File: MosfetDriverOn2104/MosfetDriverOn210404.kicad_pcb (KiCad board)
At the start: 2 copper layers, 22 parts, among them J1 Screw_Terminal_01x02, J10 CROSS CONN, J11 Screw_Terminal_01x03, J2 AVR-ISP-6, J3 I2C HDR, J4 I2C HDR, J5 UART HDR, J6 I2C HDR, J7 5V HDR, J8 ENCODER HDR, J9 GND HDR, SW1 SW_Push_Dual, SW2 SW1, SW3 SW2

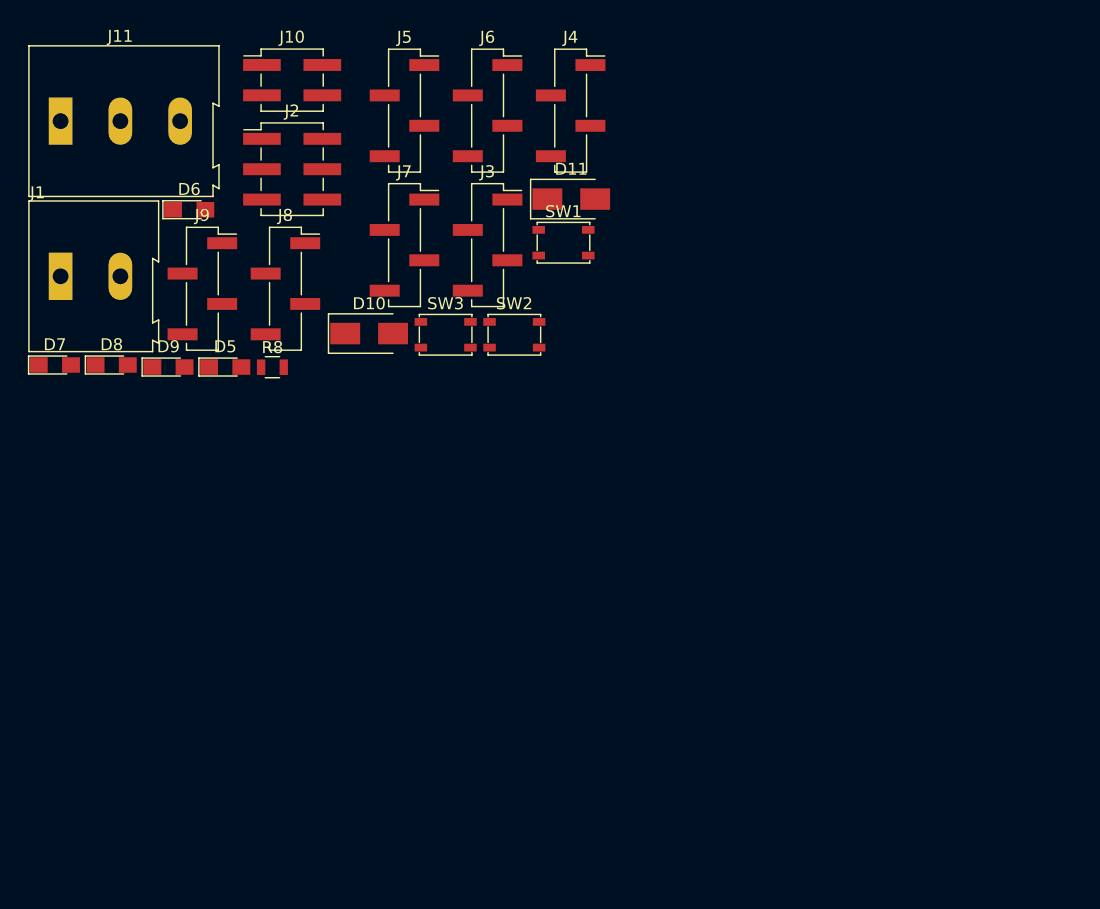
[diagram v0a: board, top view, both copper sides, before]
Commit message: #4 ,switches footprints also changed to THT
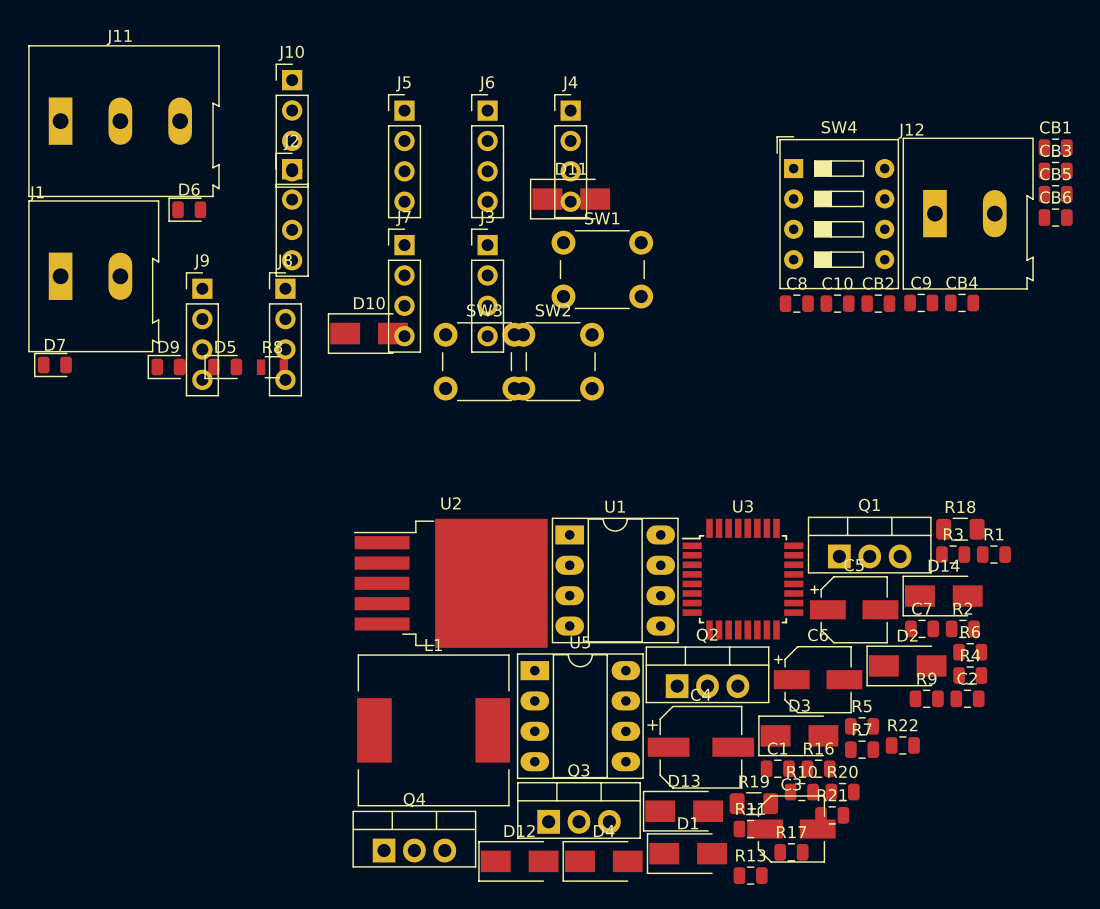
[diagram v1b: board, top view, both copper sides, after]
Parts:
- removed D8: LED, LEDs:LED_0805_HandSoldering
- added C1: C_Small, Capacitor_SMD:C_0805_2012Metric, F.Cu at (161.4, 92.3)
- added C10: 22u, Capacitor_SMD:C_0805_2012Metric, F.Cu at (166.4, 53.4)
- added C2: C_Small, Capacitor_SMD:C_0805_2012Metric, F.Cu at (177.3, 86.5)
- added C3: CP_Small, Capacitor_SMD:CP_Elec_5x4.4, F.Cu at (162.5, 97.3)
- added C4: CP, Capacitor_SMD:CP_Elec_6.3x5.7, F.Cu at (155.0, 90.5)
- added C5: CP, Capacitor_SMD:CP_Elec_5x5.4, F.Cu at (167.8, 79.0)
- added C6: CP, Capacitor_SMD:CP_Elec_5x5.4, F.Cu at (164.8, 84.9)
- added C7: C, Capacitor_SMD:C_0805_2012Metric, F.Cu at (173.5, 80.6)
- added C8: C_Small, Capacitor_SMD:C_0805_2012Metric, F.Cu at (163.0, 53.4)
- added C9: 22u, Capacitor_SMD:C_0805_2012Metric, F.Cu at (173.4, 53.3)
- added CB1: .1, Capacitor_SMD:C_0805_2012Metric, F.Cu at (184.6, 40.3)
- added CB2: .1u, Capacitor_SMD:C_0805_2012Metric, F.Cu at (169.8, 53.4)
- added CB3: 1uF, Capacitor_SMD:C_0805_2012Metric, F.Cu at (184.6, 42.3)
- added CB4: .1uF, Capacitor_SMD:C_0805_2012Metric, F.Cu at (176.8, 53.3)
- added CB5: 1uF, Capacitor_SMD:C_0805_2012Metric, F.Cu at (184.6, 44.2)
- added CB6: .1uF, Capacitor_SMD:C_0805_2012Metric, F.Cu at (184.6, 46.2)
- added D1: D, Diode_SMD:D_SMA, F.Cu at (153.9, 99.4)
- added D12: D, Diode_SMD:D_SMA, F.Cu at (139.8, 100.1)
- added D13: D, Diode_SMD:D_SMA, F.Cu at (153.6, 95.9)
- added D14: D, Diode_SMD:D_SMA, F.Cu at (175.3, 77.9)
- added D2: D, Diode_SMD:D_SMA, F.Cu at (172.3, 83.7)
- added D3: D, Diode_SMD:D_SMA, F.Cu at (163.2, 89.6)
- added D4: SS24, Diode_SMD:D_SMA, F.Cu at (146.9, 100.1)
- added J12: motor, TerminalBlock:TerminalBlock_Altech_AK300-2_P5.00mm, F.Cu at (174.6, 45.9)
- added L1: 220uH, Inductor_SMD:L_12x12mm_H6mm, F.Cu at (132.6, 89.1)
- added Q1: IRF540N, Package_TO_SOT_THT:TO-220-3_Vertical, F.Cu at (166.6, 74.5)
- added Q2: IRF540N, Package_TO_SOT_THT:TO-220-3_Vertical, F.Cu at (153.0, 85.4)
- added Q3: IRF540N, Package_TO_SOT_THT:TO-220-3_Vertical, F.Cu at (142.2, 96.7)
- added Q4: IRF540N, Package_TO_SOT_THT:TO-220-3_Vertical, F.Cu at (128.5, 99.1)
- added R1: R, Resistor_SMD:R_0805_2012Metric, F.Cu at (179.5, 74.4)
- added R10: 540, Resistor_SMD:R_0805_2012Metric, F.Cu at (163.4, 94.3)
- added R11: 540, Resistor_SMD:R_0805_2012Metric, F.Cu at (159.1, 97.3)
- added R13: 1K, Resistor_SMD:R_0805_2012Metric, F.Cu at (159.1, 101.2)
- added R16: 10K, Resistor_SMD:R_0805_2012Metric, F.Cu at (164.8, 92.3)
- added R17: R, Resistor_SMD:R_0805_2012Metric, F.Cu at (162.5, 99.3)
- added R18: R, Resistor_SMD:R_1206_3216Metric, F.Cu at (176.7, 72.3)
- added R19: R, Resistor_SMD:R_1206_3216Metric, F.Cu at (159.4, 95.2)
- added R2: R, Resistor_SMD:R_0805_2012Metric, F.Cu at (176.9, 80.6)
- added R20: R, Resistor_SMD:R_0805_2012Metric, F.Cu at (166.8, 94.3)
- added R21: R, Resistor_SMD:R_0805_2012Metric, F.Cu at (166.0, 96.2)
- added R22: R, Resistor_SMD:R_0805_2012Metric, F.Cu at (171.9, 90.4)
- added R3: 240, Resistor_SMD:R_0805_2012Metric, F.Cu at (176.1, 74.4)
- added R4: 2k7, Resistor_SMD:R_0805_2012Metric, F.Cu at (177.5, 84.5)
- added R5: 10K, Resistor_SMD:R_0805_2012Metric, F.Cu at (168.5, 88.8)
- added R6: 1K, Resistor_SMD:R_0805_2012Metric, F.Cu at (177.5, 82.6)
- added R7: 4K7, Resistor_SMD:R_0805_2012Metric, F.Cu at (168.5, 90.7)
- added R9: 540, Resistor_SMD:R_0805_2012Metric, F.Cu at (173.9, 86.5)
- added SW4: SW_DIP_x04, Button_Switch_THT:SW_DIP_SPSTx04_Slide_9.78x12.34mm_W7.62mm_P2.54mm, F.Cu at (162.7, 42.1)
- added U1: IR2104, Package_DIP:DIP-8_W7.62mm_Socket_LongPads, F.Cu at (144.0, 72.7)
- added U2: LM2576HVS-ADJ, Package_TO_SOT_SMD:TO-263-5_TabPin3, F.Cu at (134.1, 76.8)
- added U3: ATmega328P-AU-MCU_Microchip_ATmega, Package_QFP:TQFP-32_7x7mm_P0.8mm, F.Cu at (158.5, 76.4)
- added U5: IR2104, Package_DIP:DIP-8_W7.62mm_Socket_LongPads, F.Cu at (141.1, 84.1)
- D5, D6, D9: footprint LEDs:LED_0805_HandSoldering -> LED_SMD:LED_0805_2012Metric
- D7: value LED -> 5.1V; footprint LEDs:LED_0805_HandSoldering -> LED_SMD:LED_0805_2012Metric
- J10: footprint Pin_Headers:Pin_Header_Straight_2x02_Pitch2.54mm_SMD -> Connector_PinHeader_2.54mm:PinHeader_1x04_P2.54mm_Vertical
- J11: value Screw_Terminal_01x03 -> servo hdr
- J2: footprint Pin_Headers:Pin_Header_Straight_2x03_Pitch2.54mm_SMD -> Connector_PinHeader_2.54mm:PinHeader_1x04_P2.54mm_Vertical
- J3, J4, J5, J6, J7, J8, J9: footprint Pin_Headers:Pin_Header_Straight_1x04_Pitch2.54mm_SMD_Pin1Right -> Connector_PinHeader_2.54mm:PinHeader_1x04_P2.54mm_Vertical
- SW1, SW2, SW3: footprint Buttons_Switches_SMD:SW_SPST_PTS810 -> Button_Switch_THT:SW_PUSH_6mm
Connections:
- D5 pad 1: (no net) -> Net-(D5-Pad1)
- D5 pad 2: (no net) -> Net-(D5-Pad2)
- D6 pad 1: (no net) -> Net-(D6-Pad1)
- D6 pad 2: (no net) -> Net-(D6-Pad2)
- D7 pad 1: (no net) -> /~SD
- D7 pad 2: /MISO -> GND
- D9 pad 1: (no net) -> Net-(D9-Pad1)
- J1 pad 2: (no net) -> VCC
- J10 pad 2: (no net) -> /IN1
- J10 pad 3: (no net) -> /IN2
- J11 pad 1: (no net) -> GND
- J11 pad 2: GND -> /svo
- J11 pad 3: (no net) -> +5V
- J2 pad 4: (no net) -> /MOSI
- J5 pad 2: (no net) -> /TX
- J5 pad 3: (no net) -> /RX
- J8 pad 2: (no net) -> /B
- J8 pad 3: (no net) -> /A
- SW2 pad 1: Net-(R10-Pad1) -> +5V

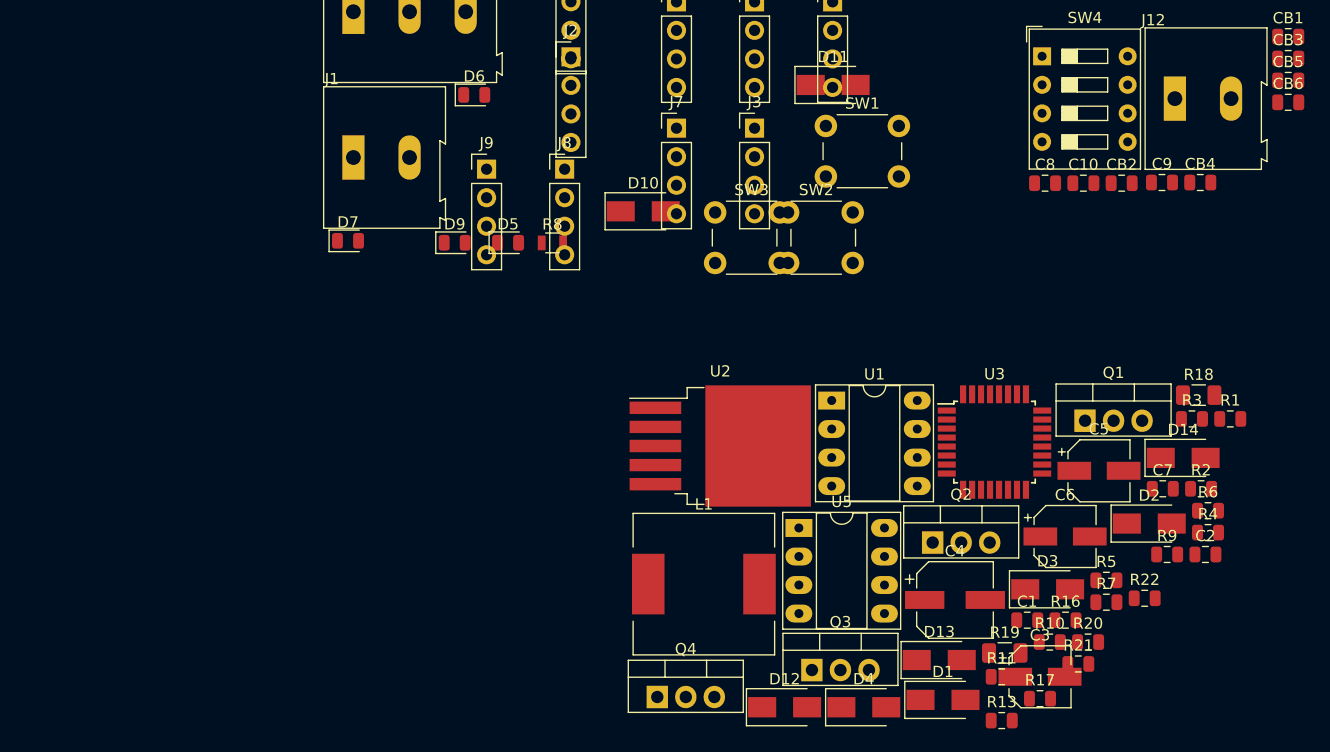
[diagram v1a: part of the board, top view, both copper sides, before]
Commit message: Schematcs updated with mosfet footprints
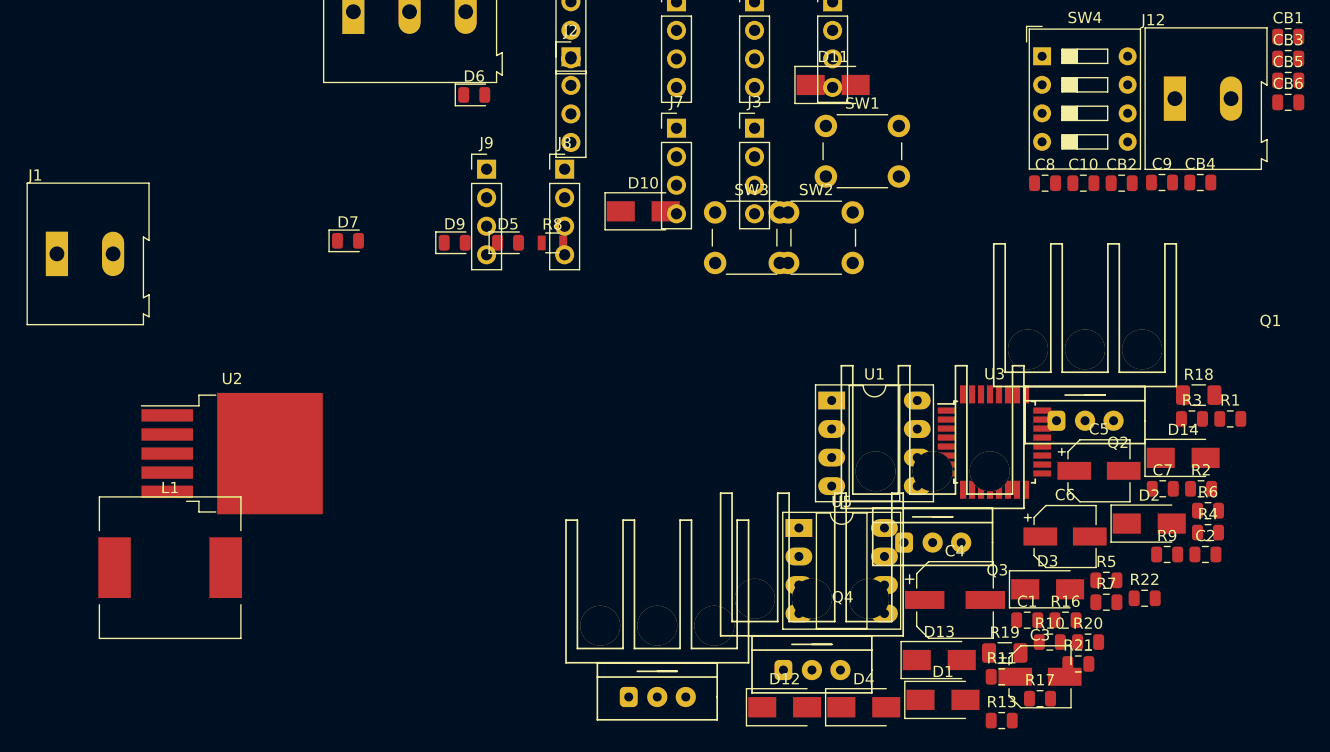
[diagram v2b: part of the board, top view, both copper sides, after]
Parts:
- Q1, Q2, Q3, Q4: footprint Package_TO_SOT_THT:TO-220-3_Vertical -> Footprints:TO220_HS_SCREW
- moved L1 47.5 mm to (85.1, 87.6)
- moved U2 43.5 mm to (90.6, 77.5)
- moved J1 27.8 mm to (75.0, 59.7)

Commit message: starting with pcb, yet to place cpmparator
i am not sure about the D2pack of 7805ic
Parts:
- removed R16: 10K, Resistor_SMD:R_0805_2012Metric
- added C11: 220uF, Capacitor_SMD:CP_Elec_5x4.4, F.Cu at (70.2, 41.9)
- added C12: 440uF, Capacitor_SMD:CP_Elec_5x4.4, F.Cu at (76.5, 48.3)
- added U4: L7805, Package_TO_SOT_SMD:TO-263-3_TabPin2, F.Cu at (230.3, 36.8)
- C8: value C_Small -> .1uF
- D7: footprint LED_SMD:LED_0805_2012Metric -> Diode_SMD:D_SMA
- J2: footprint Connector_PinHeader_2.54mm:PinHeader_1x04_P2.54mm_Vertical -> Connector_PinHeader_2.54mm:PinHeader_2x03_P2.54mm_Vertical
- SW1, SW2, SW3: footprint Button_Switch_THT:SW_PUSH_6mm -> Button_Switch_THT:SW_TH_Tactile_Omron_B3F-10xx
- moved R4 141.0 mm to (38.4, 108.0)
- moved R3 135.0 mm to (44.1, 102.9)
- moved D9 133.8 mm to (239.7, 24.1)
- moved Q3 127.7 mm to (130.8, -30.5)
- moved CB1 125.1 mm to (171.9, -84.1)
- moved CB5 125.1 mm to (171.9, -80.2)
- moved CB6 125.1 mm to (171.9, -78.3)
- moved D11 125.1 mm to (131.4, -79.8)
- moved D14 125.1 mm to (162.6, -46.6)
- moved J12 125.1 mm to (161.9, -78.6)
- moved Q1 125.1 mm to (153.9, -49.9)
- moved R1 125.1 mm to (166.8, -50.1)
- moved R17 125.1 mm to (149.8, -25.2)
- moved R18 125.1 mm to (164.0, -52.2)
- moved R22 125.1 mm to (159.2, -34.1)
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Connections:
- SW3 pad 1: Net-(R16-Pad1) -> +5V
- SW4 pad 5: +5V -> GND
- SW4 pad 6: +5V -> GND
- SW4 pad 7: +5V -> GND
- SW4 pad 8: +5V -> GND
- U3 pad 9: Net-(R16-Pad1) -> +5V
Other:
- board outline added: 99.8 x 100.6 mm

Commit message: fixes #4 , #3 ,
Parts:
- moved Q1 80.8 mm to (81.5, -14.0), turned to 180 degrees
- moved U1 61.0 mm to (70.4, -55.4)
- moved Q3 49.0 mm to (82.0, -25.9)
- moved Q2 48.7 mm to (98.6, -14.0), turned to 180 degrees
- moved D7 28.8 mm to (65.5, -48.3), turned to 270 degrees
- moved Q4 15.9 mm to (99.8, -25.4)
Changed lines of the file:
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@@
   )
   (module Package_DIP:DIP-8_W7.62mm_Socket_LongPads (layer F.Cu)
-    (at 131.295001 -51.714999)
+    (at 70.358 -55.372)
     (descr "8-lead though-hole mounted DIP package, row spacing 7.62 mm (300 mils), Socket, LongPads")
     (tags "THT DIP DIL PDIP 2.54mm 7.62mm 300mil Socket LongPads")
@@
   )
   (module Footprints:TO220_HS_SCREW (layer F.Cu)
-    (at 153.855001 -49.914999)
-    (fp_text reference Q1 (at 16.51 -8.89) (layer F.SilkS)
-      (effects (font (size 1 1) (thickness 0.15)))
-    )
-    (fp_text value IRF540N (at 2.54 -7.62) (layer F.Fab)
+    (at 81.534 -13.97 180)
+    (fp_text reference Q1 (at 16.51 -8.89 180) (layer F.SilkS)
+      (effects (font (size 1 1) (thickness 0.15)))
+    )
+    (fp_text value IRF540N (at 2.54 -7.62 180) (layer F.Fab)
       (effects (font (size 1 1) (thickness 0.15)))
     )
@@
     (fp_line (start 5.334 -3.048) (end -5.334 -3.048) (layer F.SilkS) (width 0.15))
     (fp_line (start 5.334 0) (end 5.334 -3.048) (layer F.SilkS) (width 0.15))
-    (pad 2 thru_hole circle (at 0 -6.35) (size 3.556 3.556) (drill 3.556) (layers *.Cu *.Mask)
+    (pad 2 thru_hole circle (at 0 -6.35 180) (size 3.556 3.556) (drill 3.556) (layers *.Cu *.Mask)
       (net 25 VCC))
-    (pad 2 thru_hole circle (at -5.08 -6.35) (size 3.556 3.556) (drill 3.556) (layers *.Cu *.Mask)
+    (pad 2 thru_hole circle (at -5.08 -6.35 180) (size 3.556 3.556) (drill 3.556) (layers *.Cu *.Mask)
       (net 25 VCC))
-    (pad 2 thru_hole circle (at 5.08 -6.35) (size 3.556 3.556) (drill 3.556) (layers *.Cu *.Mask)
+    (pad 2 thru_hole circle (at 5.08 -6.35 180) (size 3.556 3.556) (drill 3.556) (layers *.Cu *.Mask)
       (net 25 VCC))
-    (pad 3 thru_hole circle (at 2.54 0) (size 1.8 1.8) (drill 0.8) (layers *.Cu *.Mask)
+    (pad 3 thru_hole circle (at 2.54 0 180) (size 1.8 1.8) (drill 0.8) (layers *.Cu *.Mask)
       (net 34 /M1))
-    (pad 2 thru_hole circle (at 0 0) (size 1.8 1.8) (drill 0.8) (layers *.Cu *.Mask)
+    (pad 2 thru_hole circle (at 0 0 180) (size 1.8 1.8) (drill 0.8) (layers *.Cu *.Mask)
       (net 25 VCC))
-    (pad 1 thru_hole roundrect (at -2.54 0) (size 1.6 1.8) (drill 0.8) (layers *.Cu *.Mask) (roundrect_rratio 0.25)
+    (pad 1 thru_hole roundrect (at -2.54 0 180) (size 1.6 1.8) (drill 0.8) (layers *.Cu *.Mask) (roundrect_rratio 0.25)
       (net 11 "Net-(D2-Pad2)"))
   )
   (module Footprints:TO220_HS_SCREW (layer F.Cu)
-    (at 140.285001 -39.064999)
-    (fp_text reference Q2 (at 16.51 -8.89) (layer F.SilkS)
-      (effects (font (size 1 1) (thickness 0.15)))
-    )
-    (fp_text value IRF540N (at 2.54 -7.62) (layer F.Fab)
+    (at 98.552 -13.97 180)
+    (fp_text reference Q2 (at 16.51 -8.89 180) (layer F.SilkS)
+      (effects (font (size 1 1) (thickness 0.15)))
+    )
+    (fp_text value IRF540N (at 2.54 -7.62 180) (layer F.Fab)
       (effects (font (size 1 1) (thickness 0.15)))
     )
@@
     (fp_line (start -2.032 -4.318) (end 2.032 -4.318) (layer F.SilkS) (width 0.15))
     (fp_line (start 3.048 -4.318) (end 7.112 -4.318) (layer F.SilkS) (width 0.15))
-    (pad 1 thru_hole roundrect (at -2.54 0) (size 1.6 1.8) (drill 0.8) (layers *.Cu *.Mask) (roundrect_rratio 0.25)
+    (pad 1 thru_hole roundrect (at -2.54 0 180) (size 1.6 1.8) (drill 0.8) (layers *.Cu *.Mask) (roundrect_rratio 0.25)
       (net 14 "Net-(D3-Pad2)"))
-    (pad 2 thru_hole circle (at 0 0) (size 1.8 1.8) (drill 0.8) (layers *.Cu *.Mask)
+    (pad 2 thru_hole circle (at 0 0 180) (size 1.8 1.8) (drill 0.8) (layers *.Cu *.Mask)
       (net 34 /M1))
-    (pad 3 thru_hole circle (at 2.54 0) (size 1.8 1.8) (drill 0.8) (layers *.Cu *.Mask)
+    (pad 3 thru_hole circle (at 2.54 0 180) (size 1.8 1.8) (drill 0.8) (layers *.Cu *.Mask)
       (net 35 /IS+))
-    (pad 2 thru_hole circle (at 5.08 -6.35) (size 3.556 3.556) (drill 3.556) (layers *.Cu *.Mask)
+    (pad 2 thru_hole circle (at 5.08 -6.35 180) (size 3.556 3.556) (drill 3.556) (layers *.Cu *.Mask)
       (net 34 /M1))
-    (pad 2 thru_hole circle (at -5.08 -6.35) (size 3.556 3.556) (drill 3.556) (layers *.Cu *.Mask)
+    (pad 2 thru_hole circle (at -5.08 -6.35 180) (size 3.556 3.556) (drill 3.556) (layers *.Cu *.Mask)
       (net 34 /M1))
-    (pad 2 thru_hole circle (at 0 -6.35) (size 3.556 3.556) (drill 3.556) (layers *.Cu *.Mask)
+    (pad 2 thru_hole circle (at 0 -6.35 180) (size 3.556 3.556) (drill 3.556) (layers *.Cu *.Mask)
       (net 34 /M1))
   )
   (module Footprints:TO220_HS_SCREW (layer F.Cu)
-    (at 130.81 -30.48)
+    (at 82.042 -25.908)
     (fp_text reference Q3 (at 16.51 -8.89) (layer F.SilkS)
       (effects (font (size 1 1) (thickness 0.15)))
@@
   )
   (module Footprints:TO220_HS_SCREW (layer F.Cu)
-    (at 115.765001 -25.314999)
+    (at 99.822 -25.4)
     (fp_text reference Q4 (at 16.51 -8.89) (layer F.SilkS)
       (effects (font (size 1 1) (thickness 0.15)))
@@
   )
   (module Diode_SMD:D_SMA (layer F.Cu)
-    (at 88.227001 -65.931999)
+    (at 65.532 -48.26 270)
     (descr "Diode SMA (DO-214AC)")
     (tags "Diode SMA (DO-214AC)")
     (attr smd)
-    (fp_text reference D7 (at 0 -2.5) (layer F.SilkS)
-      (effects (font (size 1 1) (thickness 0.15)))
-    )
-    (fp_text value 5.1V (at 0 2.6) (layer F.Fab)
-      (effects (font (size 1 1) (thickness 0.15)))
-    )
-    (fp_text user %R (at 0 -2.5) (layer F.Fab)
+    (fp_text reference D7 (at 0 -2.5 270) (layer F.SilkS)
+      (effects (font (size 1 1) (thickness 0.15)))
+    )
+    (fp_text value 5.1V (at 0 2.6 270) (layer F.Fab)
+      (effects (font (size 1 1) (thickness 0.15)))
+    )
+    (fp_text user %R (at 0 -2.5 270) (layer F.Fab)
       (effects (font (size 1 1) (thickness 0.15)))
     )
@@
     (fp_line (start -3.4 1.65) (end 2 1.65) (layer F.SilkS) (width 0.12))
     (fp_line (start -3.4 -1.65) (end 2 -1.65) (layer F.SilkS) (width 0.12))
-    (pad 1 smd rect (at -2 0) (size 2.5 1.8) (layers F.Cu F.Paste F.Mask)
+    (pad 1 smd rect (at -2 0 270) (size 2.5 1.8) (layers F.Cu F.Paste F.Mask)
       (net 37 /~SD))
-    (pad 2 smd rect (at 2 0) (size 2.5 1.8) (layers F.Cu F.Paste F.Mask)
+    (pad 2 smd rect (at 2 0 270) (size 2.5 1.8) (layers F.Cu F.Paste F.Mask)
       (net 4 GND))
     (model ${KISYS3DMOD}/Diode_SMD.3dshapes/D_SMA.wrl
